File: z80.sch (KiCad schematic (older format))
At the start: 9 parts, among them P1 CONN_01X04, P2 CONN_02X20, P3 CONN_01X10, U1 7400, U1001 Z8400, U1002 AT28C64B, U1003 AS6C1008, U1004 Z8420, U1005 74LS138

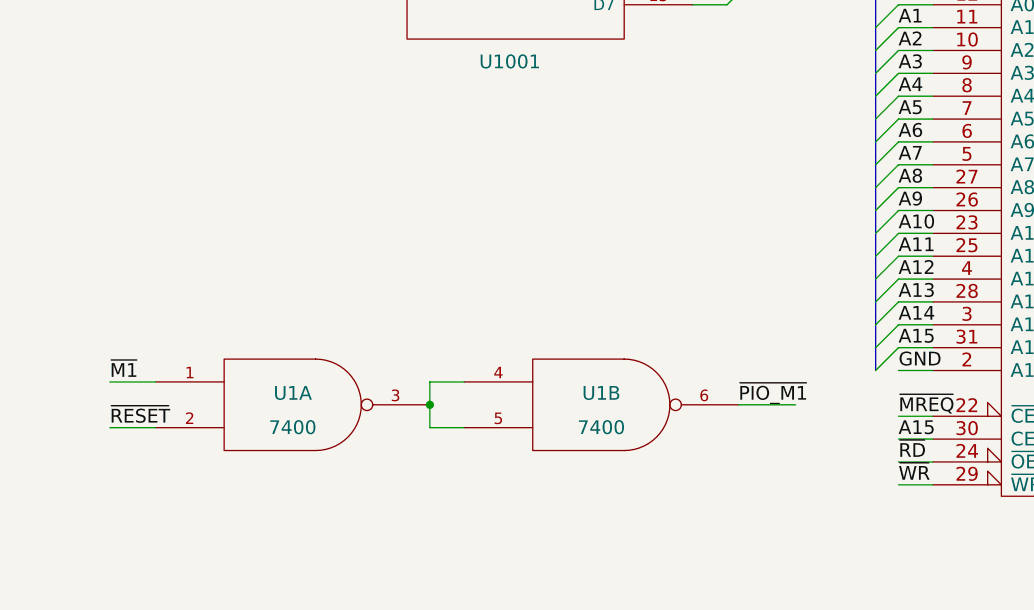
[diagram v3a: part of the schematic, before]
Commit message: More routing. Adding decoupling and ~INT pull-up
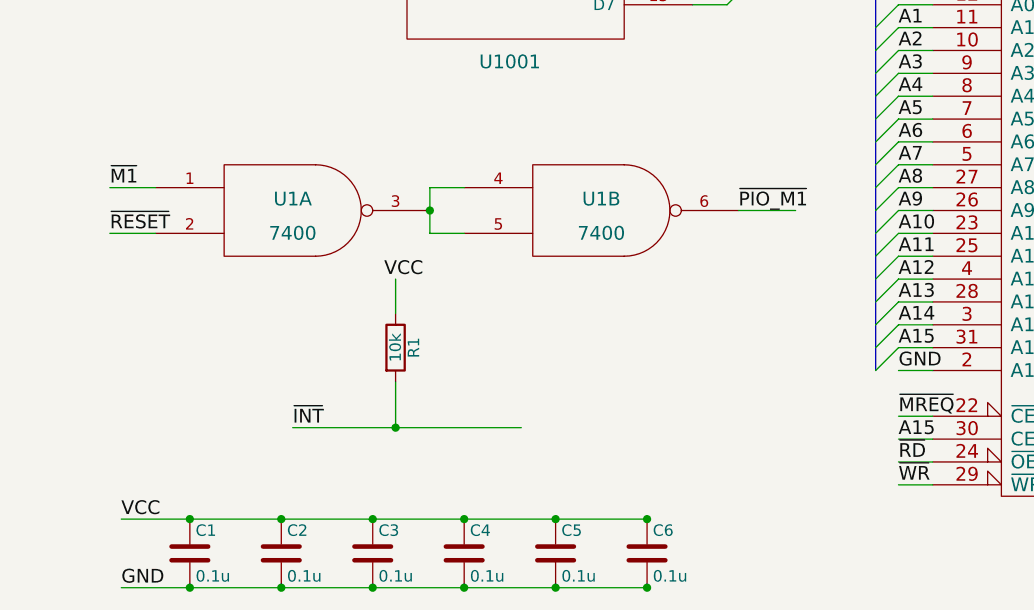
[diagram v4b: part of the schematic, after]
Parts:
- added C1, C2, C3, C4, C5, C6: 0.1u, symbol C
- added R1: 10k, symbol R
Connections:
- wire segments 191 -> 196
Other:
- moved on the sheet: U1A, U1B
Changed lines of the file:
@@
 L 7400 U1
 U 1 1 5503FD72
-P 1850 5850
-F 0 "U1" H 1850 5900 60  0000 C CNN
-F 1 "7400" H 1850 5750 60  0000 C CNN
-F 2 "" H 1850 5850 60  0000 C CNN
-F 3 "" H 1850 5850 60  0000 C CNN
-	1    1850 5850
+P 1850 5000
+F 0 "U1" H 1850 5050 60  0000 C CNN
+F 1 "7400" H 1850 4900 60  0000 C CNN
+F 2 "" H 1850 5000 60  0000 C CNN
+F 3 "" H 1850 5000 60  0000 C CNN
+	1    1850 5000
 	1    0    0    -1
 $EndComp
@@
 L 7400 U1
 U 2 1 5503FD9E
-P 3200 5850
-F 0 "U1" H 3200 5900 60  0000 C CNN
-F 1 "7400" H 3200 5750 60  0000 C CNN
-F 2 "" H 3200 5850 60  0000 C CNN
-F 3 "" H 3200 5850 60  0000 C CNN
-	2    3200 5850
-	1    0    0    -1
-$EndComp
-Wire Wire Line
-	2450 5750 2450 5950
-Wire Wire Line
-	2450 5750 2600 5750
-Wire Wire Line
-	2450 5950 2600 5950
-Connection ~ 2450 5850
-Wire Wire Line
-	1050 5750 1250 5750
-Text Label 1050 5750 0    60   ~ 0
+P 3200 5000
+F 0 "U1" H 3200 5050 60  0000 C CNN
+F 1 "7400" H 3200 4900 60  0000 C CNN
+F 2 "" H 3200 5000 60  0000 C CNN
+F 3 "" H 3200 5000 60  0000 C CNN
+	2    3200 5000
+	1    0    0    -1
+$EndComp
+Wire Wire Line
+	2450 4900 2450 5100
+Wire Wire Line
+	2450 4900 2600 4900
+Wire Wire Line
+	2450 5100 2600 5100
+Connection ~ 2450 5000
+Wire Wire Line
+	1050 4900 1250 4900
+Text Label 1050 4900 0    60   ~ 0
 ~M1
 Wire Wire Line
-	1050 5950 1250 5950
-Text Label 1050 5950 0    60   ~ 0
+	1050 5100 1250 5100
+Text Label 1050 5100 0    60   ~ 0
 ~RESET
 Wire Wire Line
-	3800 5850 4050 5850
-Text Label 3800 5850 0    60   ~ 0
+	3800 5000 4050 5000
+Text Label 3800 5000 0    60   ~ 0
 ~PIO_M1
 $Comp
@@
 Text Label 10450 5050 0    60   ~ 0
 ~CE_2
+$Comp
+L R R1
+U 1 1 550E7B87
+P 2300 5600
+F 0 "R1" V 2380 5600 50  0000 C CNN
+F 1 "10k" V 2300 5600 50  0000 C CNN
+F 2 "" V 2230 5600 30  0000 C CNN
+F 3 "" H 2300 5600 30  0000 C CNN
+	1    2300 5600
+	1    0    0    -1
+$EndComp
+Wire Wire Line
+	2300 5750 2300 5950
+Wire Wire Line
+	1850 5950 2850 5950
+Connection ~ 2300 5950
+Wire Wire Line
+	2300 5300 2300 5450
+Text Label 2250 5300 0    60   ~ 0
+VCC
+Text Label 1850 5950 0    60   ~ 0
+~INT
+$Comp
+L C C1
+U 1 1 550E845D
+P 1400 6500
+F 0 "C1" H 1425 6600 50  0000 L CNN
+F 1 "0.1u" H 1425 6400 50  0000 L CNN
+F 2 "" H 1438 6350 30  0000 C CNN
+F 3 "" H 1400 6500 60  0000 C CNN
+	1    1400 6500
+	1    0    0    -1
+$EndComp
+$Comp
+L C C2
+U 1 1 550E84A5
+P 1800 6500
+F 0 "C2" H 1825 6600 50  0000 L CNN
+F 1 "0.1u" H 1825 6400 50  0000 L CNN
+F 2 "" H 1838 6350 30  0000 C CNN
+F 3 "" H 1800 6500 60  0000 C CNN
+	1    1800 6500
+	1    0    0    -1
+$EndComp
+$Comp
+L C C3
+U 1 1 550E84E2
+P 2200 6500
+F 0 "C3" H 2225 6600 50  0000 L CNN
+F 1 "0.1u" H 2225 6400 50  0000 L CNN
+F 2 "" H 2238 6350 30  0000 C CNN
+F 3 "" H 2200 6500 60  0000 C CNN
+	1    2200 6500
+	1    0    0    -1
+$EndComp
+$Comp
+L C C4
+U 1 1 550E855B
+P 2600 6500
+F 0 "C4" H 2625 6600 50  0000 L CNN
+F 1 "0.1u" H 2625 6400 50  0000 L CNN
+F 2 "" H 2638 6350 30  0000 C CNN
+F 3 "" H 2600 6500 60  0000 C CNN
+	1    2600 6500
+	1    0    0    -1
+$EndComp
+$Comp
+L C C5
+U 1 1 550E8561
+P 3000 6500
+F 0 "C5" H 3025 6600 50  0000 L CNN
+F 1 "0.1u" H 3025 6400 50  0000 L CNN
+F 2 "" H 3038 6350 30  0000 C CNN
+F 3 "" H 3000 6500 60  0000 C CNN
+	1    3000 6500
+	1    0    0    -1
+$EndComp
+$Comp
+L C C6
+U 1 1 550E8567
+P 3400 6500
+F 0 "C6" H 3425 6600 50  0000 L CNN
+F 1 "0.1u" H 3425 6400 50  0000 L CNN
+F 2 "" H 3438 6350 30  0000 C CNN
+F 3 "" H 3400 6500 60  0000 C CNN
+	1    3400 6500
+	1    0    0    -1
+$EndComp
+Wire Wire Line
+	1100 6350 3400 6350
+Wire Wire Line
+	1100 6650 3400 6650
+Connection ~ 3000 6650
+Connection ~ 2600 6650
+Connection ~ 2200 6650
+Connection ~ 1800 6650
+Connection ~ 1400 6650
+Connection ~ 1400 6350
+Connection ~ 3400 6650
+Connection ~ 3400 6350
+Connection ~ 3000 6350
+Connection ~ 2600 6350
+Connection ~ 2200 6350
+Connection ~ 1800 6350
+Text Label 1100 6350 0    60   ~ 0
+VCC
+Text Label 1100 6650 0    60   ~ 0
+GND
 $EndSCHEMATC

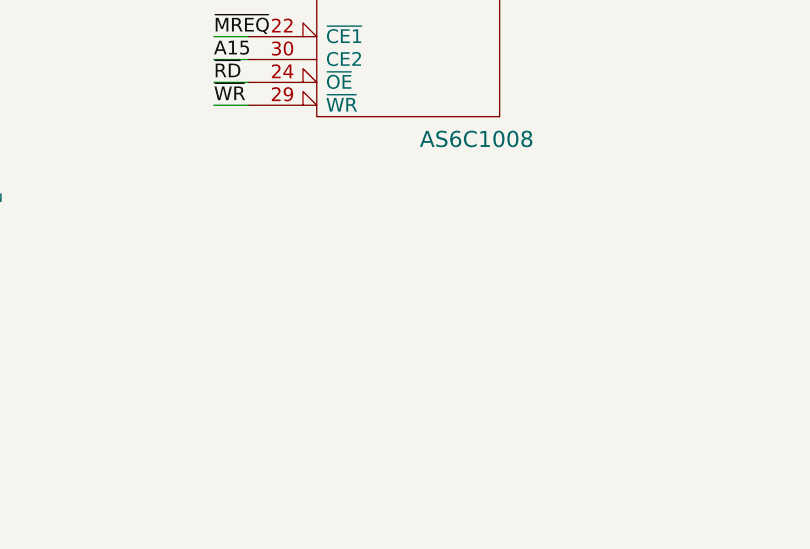
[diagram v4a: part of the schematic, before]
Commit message: Add crystal clock circuit
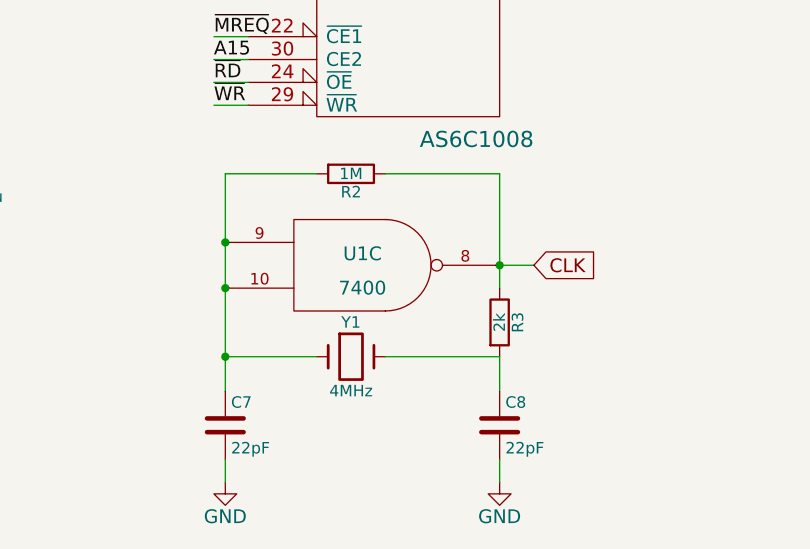
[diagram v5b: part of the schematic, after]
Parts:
- added C7, C8: 22pF, symbol C
- added R2: 1M, symbol R
- added R3: 2k, symbol R
- added unit 3 of U1
- added Y1: 4MHz, symbol Crystal
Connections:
- wire segments 196 -> 206
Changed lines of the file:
@@
 Text Label 1100 6650 0    60   ~ 0
 GND
+$Comp
+L 7400 U1
+U 3 1 56759306
+P 5150 6900
+F 0 "U1" H 5150 6950 60  0000 C CNN
+F 1 "7400" H 5150 6800 60  0000 C CNN
+F 2 "" H 5150 6900 60  0000 C CNN
+F 3 "" H 5150 6900 60  0000 C CNN
+	3    5150 6900
+	1    0    0    -1
+$EndComp
+$Comp
+L R R3
+U 1 1 567593B2
+P 5750 7150
+F 0 "R3" V 5830 7150 50  0000 C CNN
+F 1 "2k" V 5750 7150 50  0000 C CNN
+F 2 "" V 5680 7150 30  0000 C CNN
+F 3 "" H 5750 7150 30  0000 C CNN
+	1    5750 7150
+	1    0    0    -1
+$EndComp
+$Comp
+L C C8
+U 1 1 5675940A
+P 5750 7600
+F 0 "C8" H 5775 7700 50  0000 L CNN
+F 1 "22pF" H 5775 7500 50  0000 L CNN
+F 2 "" H 5788 7450 30  0000 C CNN
+F 3 "" H 5750 7600 60  0000 C CNN
+	1    5750 7600
+	1    0    0    -1
+$EndComp
+$Comp
+L C C7
+U 1 1 5675946B
+P 4550 7600
+F 0 "C7" H 4575 7700 50  0000 L CNN
+F 1 "22pF" H 4575 7500 50  0000 L CNN
+F 2 "" H 4588 7450 30  0000 C CNN
+F 3 "" H 4550 7600 60  0000 C CNN
+	1    4550 7600
+	1    0    0    -1
+$EndComp
+$Comp
+L Crystal Y1
+U 1 1 567594FC
+P 5100 7300
+F 0 "Y1" H 5100 7450 50  0000 C CNN
+F 1 "4MHz" H 5100 7150 50  0000 C CNN
+F 2 "" H 5100 7300 60  0000 C CNN
+F 3 "" H 5100 7300 60  0000 C CNN
+	1    5100 7300
+	1    0    0    -1
+$EndComp
+$Comp
+L R R2
+U 1 1 5675953C
+P 5100 6500
+F 0 "R2" V 5180 6500 50  0000 C CNN
+F 1 "1M" V 5100 6500 50  0000 C CNN
+F 2 "" V 5030 6500 30  0000 C CNN
+F 3 "" H 5100 6500 30  0000 C CNN
+	1    5100 6500
+	0    1    1    0
+$EndComp
+Wire Wire Line
+	5250 6500 5750 6500
+Wire Wire Line
+	5750 6500 5750 7000
+Connection ~ 5750 6900
+Wire Wire Line
+	5750 7300 5750 7450
+Wire Wire Line
+	5750 7300 5250 7300
+Wire Wire Line
+	4550 7300 4950 7300
+Wire Wire Line
+	4550 6500 4550 7450
+Connection ~ 4550 7000
+Wire Wire Line
+	4550 6500 4950 6500
+Connection ~ 4550 6800
+Connection ~ 4550 7300
+$Comp
+L GND #PWR2
+U 1 1 56759EC1
+P 5750 7850
+F 0 "#PWR2" H 5750 7600 60  0001 C CNN
+F 1 "GND" H 5750 7700 60  0000 C CNN
+F 2 "" H 5750 7850 60  0000 C CNN
+F 3 "" H 5750 7850 60  0000 C CNN
+	1    5750 7850
+	1    0    0    -1
+$EndComp
+$Comp
+L GND #PWR1
+U 1 1 56759F03
+P 4550 7850
+F 0 "#PWR1" H 4550 7600 60  0001 C CNN
+F 1 "GND" H 4550 7700 60  0000 C CNN
+F 2 "" H 4550 7850 60  0000 C CNN
+F 3 "" H 4550 7850 60  0000 C CNN
+	1    4550 7850
+	1    0    0    -1
+$EndComp
+Wire Wire Line
+	4550 7750 4550 7850
+Wire Wire Line
+	5750 7750 5750 7850
+Wire Wire Line
+	5900 6900 5750 6900
+Text GLabel 5900 6900 2    60   Input ~ 0
+CLK
 $EndSCHEMATC
